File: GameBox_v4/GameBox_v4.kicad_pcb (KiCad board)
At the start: 2 copper layers, 35.5 x 75.5 mm, 22 parts, among them J1 OLED, J2 Conn_01x08, SW1 ON/OFF, SW2 SW_up, SW3 SW_down, SW4 SW_right, SW5 SW_left, SW6 SW_select, U1 ATmega328P-A, U2 3.3V_boost_regulator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

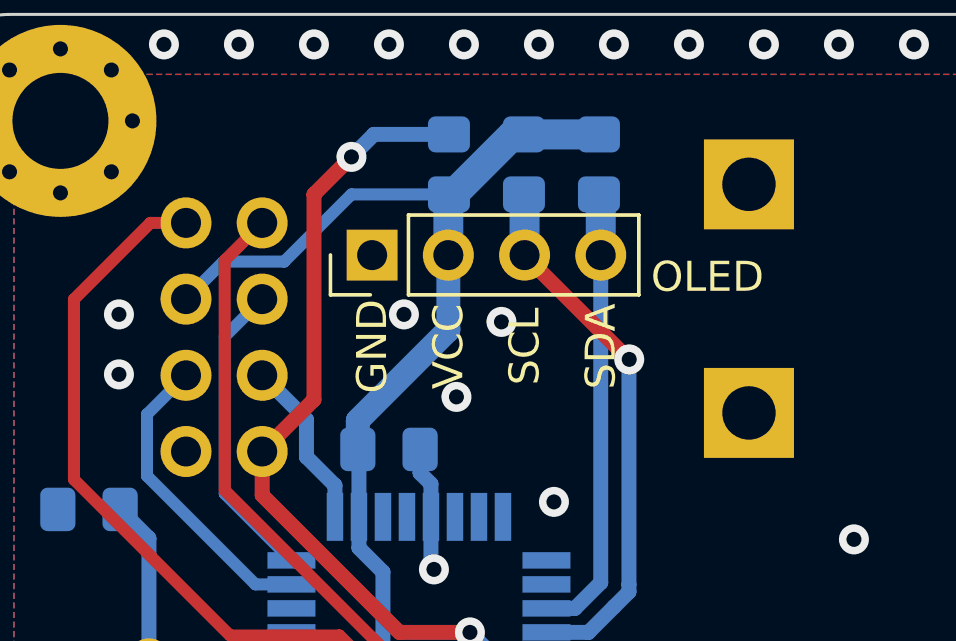
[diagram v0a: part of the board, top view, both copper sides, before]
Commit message: fixed OLEDs
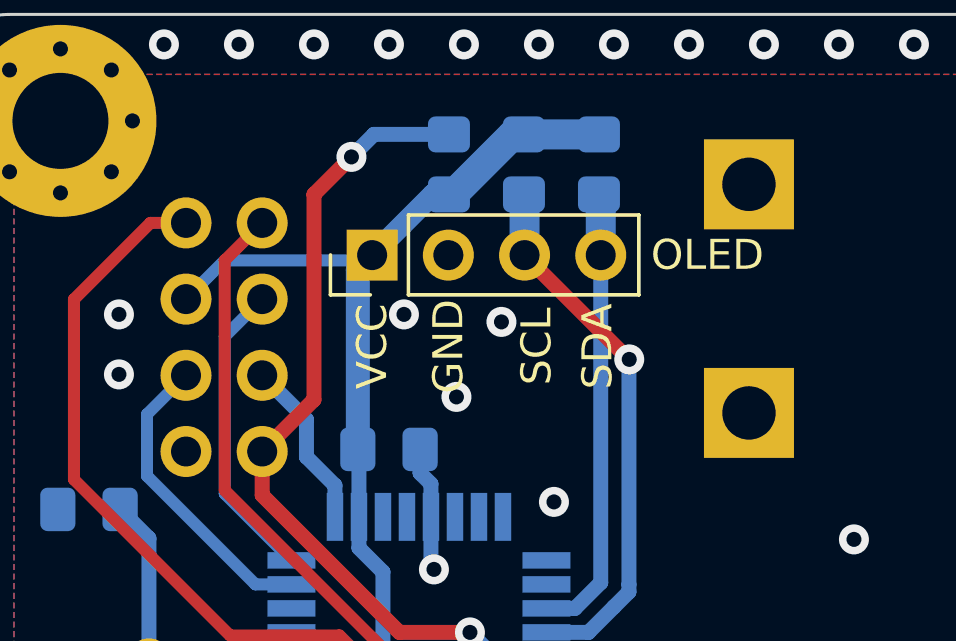
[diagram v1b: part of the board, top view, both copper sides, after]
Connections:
- J1 pad 1: GND -> VCC
- J1 pad 2: VCC -> GND
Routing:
- net VCC: track 55.7 -> 52.6 mm
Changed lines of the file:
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@@
       (effects (font (size 1 1) (thickness 0.15)))
     )
-    (fp_text user "SCL" (at 1.27 -11.684 90 unlocked) (layer "F.SilkS")
+    (fp_text user "GND" (at -1.27 -11.684 90 unlocked) (layer "F.SilkS")
       (effects (font (size 1 1) (thickness 0.15)))
     )
-    (fp_text user "VCC" (at -1.27 -11.684 90 unlocked) (layer "F.SilkS")
+    (fp_text user "OLED" (at 7.366 -14.732 unlocked) (layer "F.SilkS")
       (effects (font (size 1 1) (thickness 0.15)))
     )
-    (fp_text user "SDA" (at 3.81 -11.684 90 unlocked) (layer "F.SilkS")
+    (fp_text user "SCL" (at 1.668 -11.684 90 unlocked) (layer "F.SilkS")
       (effects (font (size 1 1) (thickness 0.15)))
     )
-    (fp_text user "GND" (at -3.81 -11.684 90 unlocked) (layer "F.SilkS")
+    (fp_text user "VCC" (at -3.81 -11.684 90 unlocked) (layer "F.SilkS")
       (effects (font (size 1 1) (thickness 0.15)))
     )
-    (fp_text user "OLED" (at 7.366 -14 unlocked) (layer "F.SilkS")
+    (fp_text user "SDA" (at 3.7 -11.684 90 unlocked) (layer "F.SilkS")
       (effects (font (size 1 1) (thickness 0.15)))
     )
@@
       (effects (font (size 1 1) (thickness 0.15)))
     )
+    (fp_line (start -3.87 -13.402) (end -5.2 -13.402) (layer "F.SilkS") (width 0.12))
+    (fp_line (start -2.6 -13.402) (end -2.6 -16.062) (layer "F.SilkS") (width 0.12))
+    (fp_line (start 5.08 -13.402) (end 5.08 -16.062) (layer "F.SilkS") (width 0.12))
     (fp_line (start -2.6 -16.062) (end 5.08 -16.062) (layer "F.SilkS") (width 0.12))
-    (fp_line (start 5.08 -13.402) (end 5.08 -16.062) (layer "F.SilkS") (width 0.12))
     (fp_line (start -2.6 -13.402) (end 5.08 -13.402) (layer "F.SilkS") (width 0.12))
-    (fp_line (start -2.6 -13.402) (end -2.6 -16.062) (layer "F.SilkS") (width 0.12))
     (fp_line (start -5.2 -13.402) (end -5.2 -14.732) (layer "F.SilkS") (width 0.12))
-    (fp_line (start -3.87 -13.402) (end -5.2 -13.402) (layer "F.SilkS") (width 0.12))
+    (fp_line (start -16.764 -16.22) (end 16.764 -16.22) (layer "F.CrtYd") (width 0.05))
     (fp_line (start 16.764 17.69) (end 7 17.69) (layer "F.CrtYd") (width 0.05))
+    (fp_line (start -7 13.69) (end -7 17.69) (layer "F.CrtYd") (width 0.05))
+    (fp_line (start -16.764 17.69) (end -16.764 -16.22) (layer "F.CrtYd") (width 0.05))
+    (fp_line (start -7 17.69) (end -16.764 17.69) (layer "F.CrtYd") (width 0.05))
+    (fp_line (start 16.764 -16.22) (end 16.764 17.69) (layer "F.CrtYd") (width 0.05))
     (fp_line (start 7 13.69) (end 7 17.69) (layer "F.CrtYd") (width 0.05))
-    (fp_line (start -7 13.69) (end -7 17.69) (layer "F.CrtYd") (width 0.05))
-    (fp_line (start 16.764 -16.22) (end 16.764 17.69) (layer "F.CrtYd") (width 0.05))
-    (fp_line (start -7 17.69) (end -16.764 17.69) (layer "F.CrtYd") (width 0.05))
-    (fp_line (start -16.764 17.69) (end -16.764 -16.22) (layer "F.CrtYd") (width 0.05))
     (fp_line (start -7 13.69) (end 7 13.69) (layer "F.CrtYd") (width 0.05))
-    (fp_line (start -16.764 -16.22) (end 16.764 -16.22) (layer "F.CrtYd") (width 0.05))
     (pad "1" thru_hole rect (at -3.81 -14.726 90) (size 1.7 1.7) (drill 1) (layers *.Cu *.Mask)
-      (net 7 "GND") (pinfunction "Pin_1") (pintype "passive"))
+      (net 1 "VCC") (pinfunction "Pin_1") (pintype "passive"))
     (pad "2" thru_hole oval (at -1.27 -14.726 90) (size 1.7 1.7) (drill 1) (layers *.Cu *.Mask)
-      (net 1 "VCC") (pinfunction "Pin_2") (pintype "passive"))
+      (net 7 "GND") (pinfunction "Pin_2") (pintype "passive"))
     (pad "3" thru_hole oval (at 1.27 -14.726 90) (size 1.7 1.7) (drill 1) (layers *.Cu *.Mask)
       (net 3 "SCL") (pinfunction "Pin_3") (pintype "passive"))
@@
   (segment (start 166.48 81.02) (end 166.5 81) (width 1) (layer "B.Cu") (net 1))
   (segment (start 164.5 103.2125) (end 160.658478 103.2125) (width 1) (layer "B.Cu") (net 1))
+  (segment (start 163.764489 83.199511) (end 163.94 83.024) (width 0.4) (layer "B.Cu") (net 1))
   (segment (start 164.3 101.562) (end 164.3 103.0125) (width 0.5) (layer "B.Cu") (net 1))
   (segment (start 169 79) (end 168.5 79) (width 0.5) (layer "B.Cu") (net 1))
-  (segment (start 163.4625 88.5375) (end 166.48 85.52) (width 0.8) (layer "B.Cu") (net 1))
-  (segment (start 166.48 85.52) (end 166.48 83.024) (width 0.8) (layer "B.Cu") (net 1))
-  (segment (start 166.48 83.024) (end 166.48 81.02) (width 1) (layer "B.Cu") (net 1))
-  (segment (start 161.009511 83.240489) (end 163.25 81) (width 0.4) (layer "B.Cu") (net 1))
-  (segment (start 163.4625 89.5) (end 163.4625 88.5375) (width 0.8) (layer "B.Cu") (net 1))
+  (segment (start 159.025489 83.199511) (end 163.764489 83.199511) (width 0.4) (layer "B.Cu") (net 1))
   (segment (start 166.642824 81) (end 168.642824 79) (width 1) (layer "B.Cu") (net 1))
   (segment (start 163.5 91.75) (end 163.5 89.5375) (width 0.5) (layer "B.Cu") (net 1))
-  (segment (start 163.25 81) (end 166.5 81) (width 0.4) (layer "B.Cu") (net 1))
   (segment (start 163.5 92.785489) (end 163.5 91.75) (width 0.5) (layer "B.Cu") (net 1))
   (segment (start 165.9 101.4) (end 166.5 102) (width 0.5) (layer "B.Cu") (net 1))
+  (segment (start 165.964 81) (end 163.94 83.024) (width 0.7) (layer "B.Cu") (net 1))
   (segment (start 168.642824 79) (end 169 79) (width 1) (layer "B.Cu") (net 1))
+  (segment (start 163.4625 89.5) (end 163.4625 83.5015) (width 0.8) (layer "B.Cu") (net 1))
   (segment (start 164.3 93.585489) (end 163.5 92.785489) (width 0.5) (layer "B.Cu") (net 1))
   (segment (start 160.658478 103.2125) (end 159.23 104.640978) (width 1) (layer "B.Cu") (net 1))
@@
   (segment (start 166.5 102) (end 166.5 103.2125) (width 0.5) (layer "B.Cu") (net 1))
   (segment (start 164.3 103.0125) (end 164.5 103.2125) (width 0.5) (layer "B.Cu") (net 1))
-  (segment (start 158.984511 83.240489) (end 161.009511 83.240489) (width 0.4) (layer "B.Cu") (net 1))
+  (segment (start 166.5 81) (end 165.964 81) (width 0.7) (layer "B.Cu") (net 1))
   (segment (start 159.23 104.640978) (end 159.23 106.045) (width 1) (layer "B.Cu") (net 1))
+  (segment (start 163.4625 83.5015) (end 163.94 83.024) (width 0.8) (layer "B.Cu") (net 1))
   (segment (start 171.5 79) (end 169 79) (width 1) (layer "B.Cu") (net 1))
-  (segment (start 157.735 84.49) (end 158.984511 83.240489) (width 0.4) (layer "B.Cu") (net 1))
   (segment (start 164.3 100.25) (end 164.3 101.562) (width 0.5) (layer "B.Cu") (net 1))
+  (segment (start 157.735 84.49) (end 159.025489 83.199511) (width 0.4) (layer "B.Cu") (net 1))
   (segment (start 164.3 100.25) (end 164.3 93.585489) (width 0.5) (layer "B.Cu") (net 1))
   (segment (start 168.5 79) (end 166.5 81) (width 0.5) (layer "B.Cu") (net 1))
